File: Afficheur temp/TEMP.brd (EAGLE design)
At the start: 82 x 40 mm, 24 parts, among them IC1 MCP23008P, IC2 MCP23008P, X1 22-23-2041

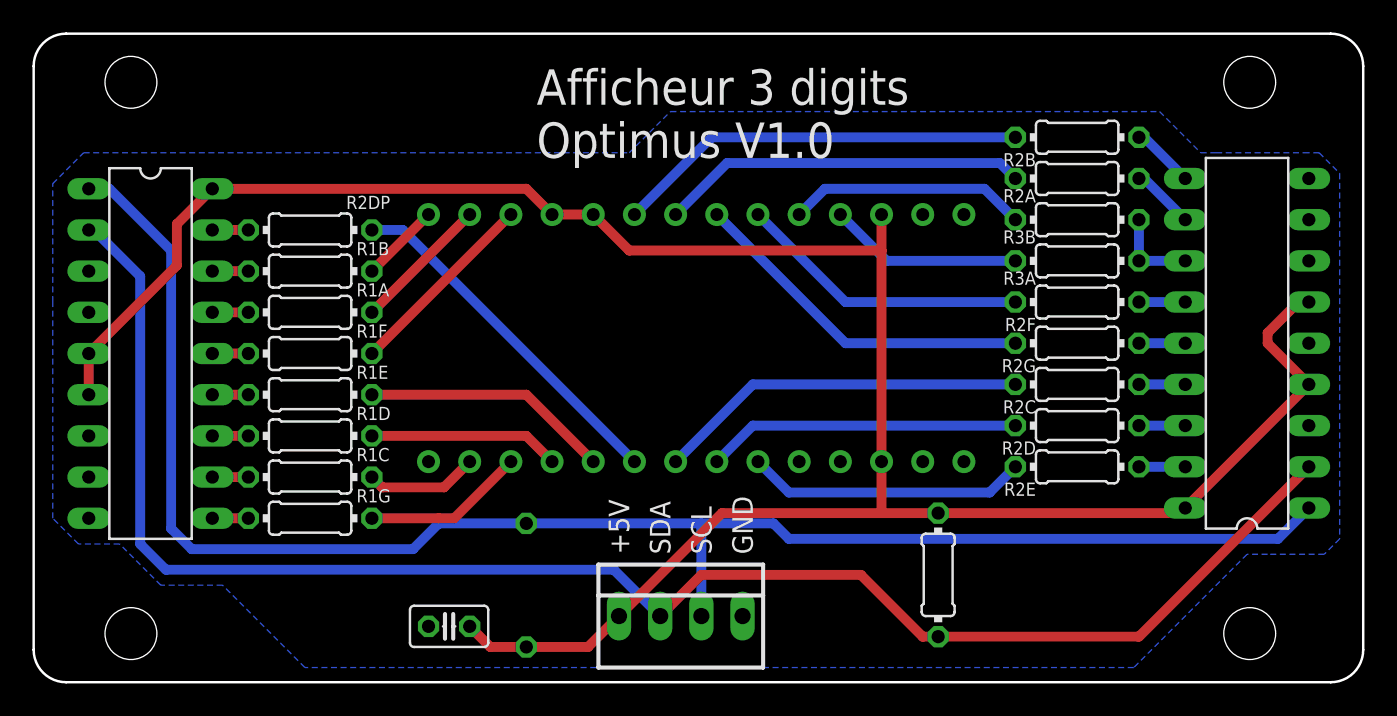
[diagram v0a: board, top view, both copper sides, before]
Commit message: Supprsion des résistance de pull-up et MAJ des condos de lissage
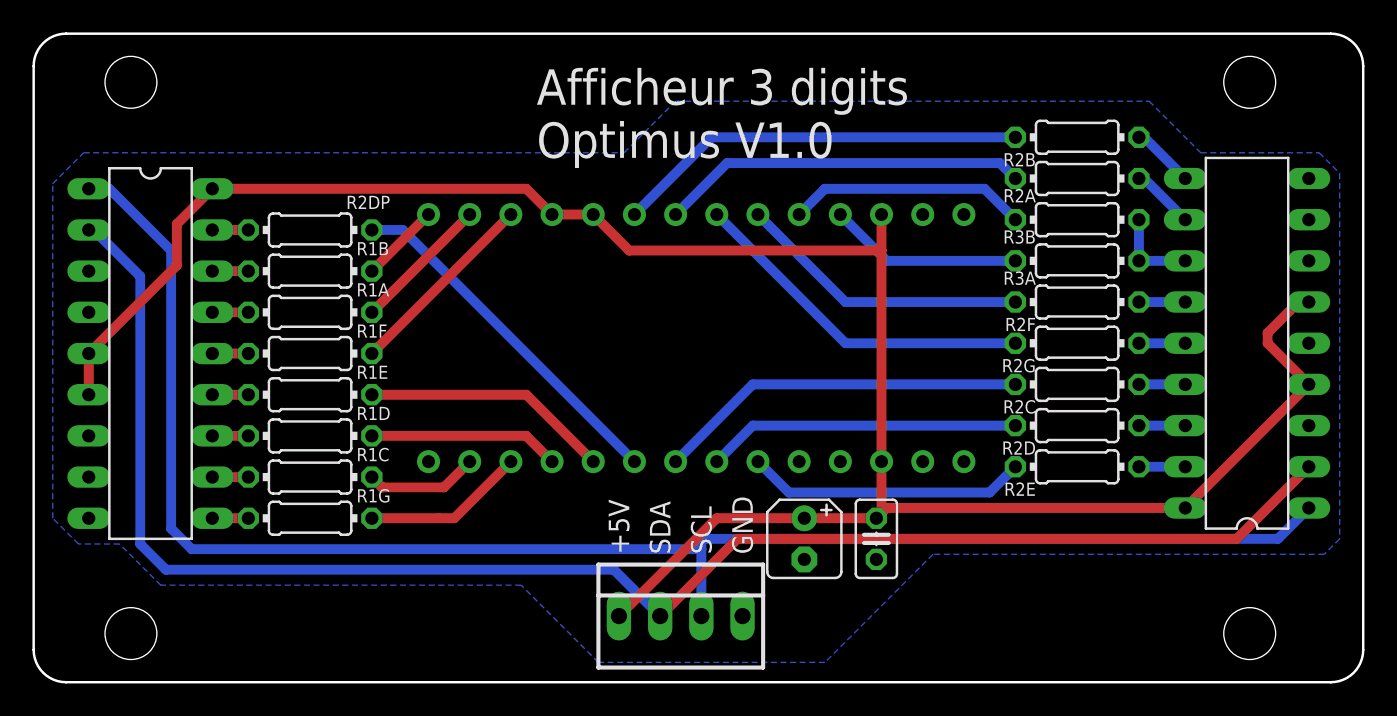
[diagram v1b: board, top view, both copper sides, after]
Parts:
- removed R1, R2: 1k, rcl:0204/7
- added C6: 500pF, rcl:C025-025X050
- C1: value 500pF -> 1µF; device rcl:C025-025X050 -> resistor:B45181A
- moved C1 22.6 mm to (49.5, 9.84), turned to 270 degrees
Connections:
- net +5V: now also C1.+, C6.1; no longer C1.1, R1.2, R2.1
- net GND: now also C1.-, C6.2; no longer C1.2
- net SCL: no longer R1.1
- net SDA: no longer R2.2
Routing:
- net +5V: track 143.7 -> 133.1 mm
- net SDA: track 101.8 -> 98.6 mm
- net SCL: track 102.1 -> 100.0 mm
